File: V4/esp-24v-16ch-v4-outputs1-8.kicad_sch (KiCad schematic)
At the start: 5 parts, among them Q4 MMBT2222A

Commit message: Revising the schematics
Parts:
- R26: value 10k/62,5mW -> 10k
- R27: value 1k/62,5mW -> 1k
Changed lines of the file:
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@@
 			)
 		)
-		(property "Value" "1k/62,5mW"
+		(property "Value" "1k"
 			(at 125.73 99.06 90)
 			(effects
@@
 			)
 		)
-		(property "Value" "10k/62,5mW"
+		(property "Value" "10k"
 			(at 110.49 110.49 0)
 			(effects

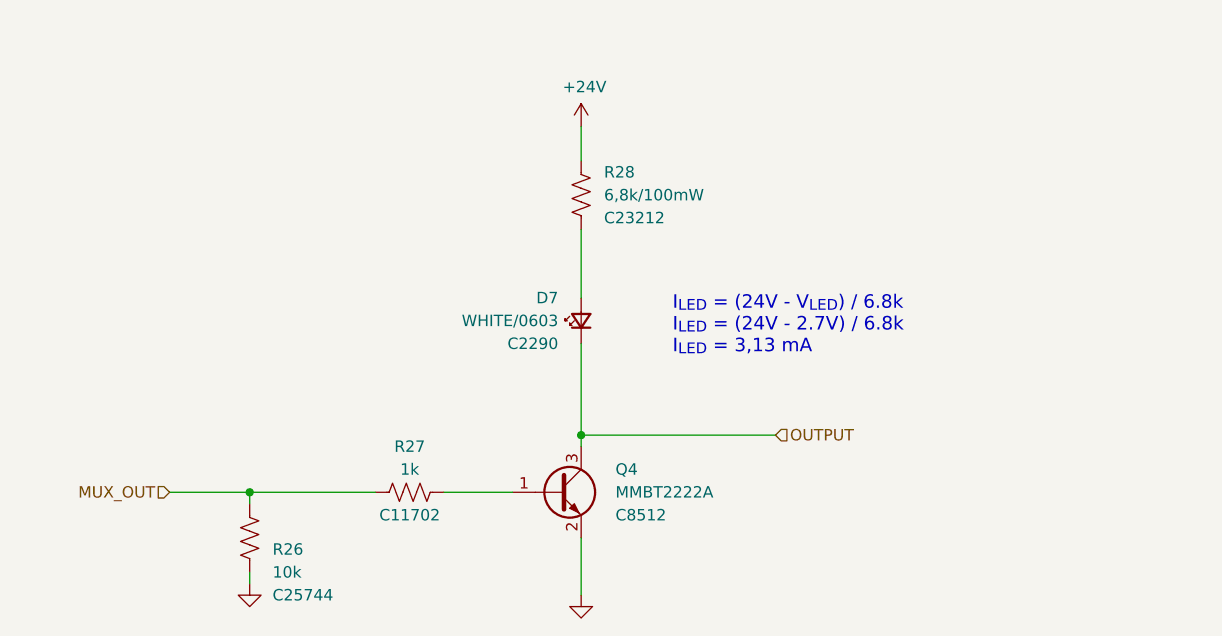
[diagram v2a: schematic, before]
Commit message: Rerouting
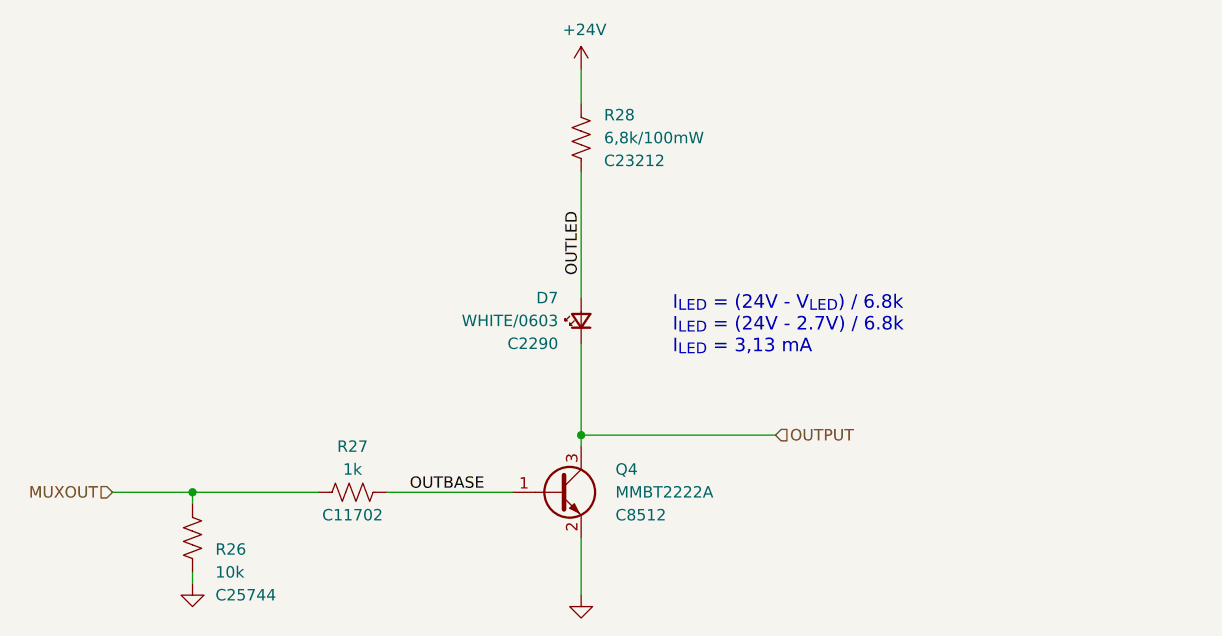
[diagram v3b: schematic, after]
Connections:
- net OUTLED: now reaches D7.2 (A), R28.2
- net OUTBASE: now reaches Q4.1 (B), R27.1
- net MUX_OUT renamed MUXOUT
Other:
- moved on the sheet: R26, R27, R28

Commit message: Rerouting
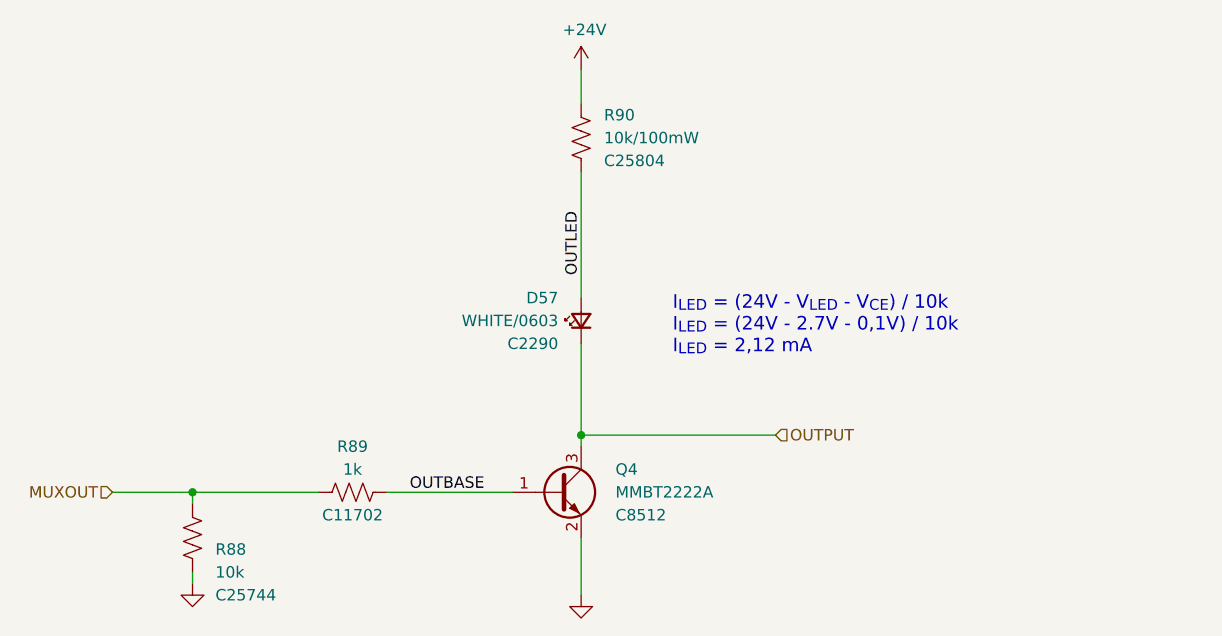
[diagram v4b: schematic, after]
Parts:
- R90: renamed from R28; value 6,8k/100mW -> 10k/100mW; LCSC Part # C23212 -> C25804; Mfr PN 0603WAF6801T5E -> 0603WAF1002T5E; Vendor PN C23212 -> C25804
- renumbered D7 to D57, R26 to R88, R27 to R89
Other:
- note added: "I_{LED} = (24V - V_{LED} - V_{CE}) / 10k I_{LED} = (24V - 2.7V - 0,1V) / 10k I_{LED} = 2,12 mA"
- note removed: "I_{LED} = (24V - V_{LED}) / 6.8k I_{LED} = (24V - 2.7V) / 6.8k I_{LED} = 3,13 mA"
